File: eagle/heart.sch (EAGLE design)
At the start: 8 parts

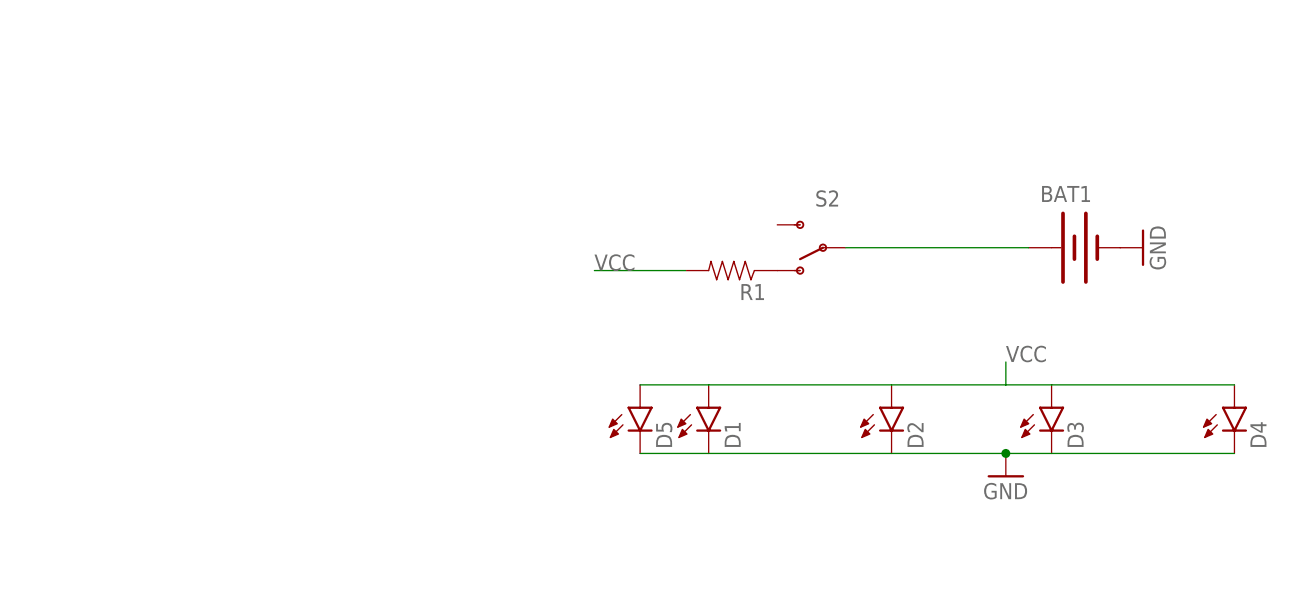
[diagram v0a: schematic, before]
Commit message: move eagle files to `eagle` dir
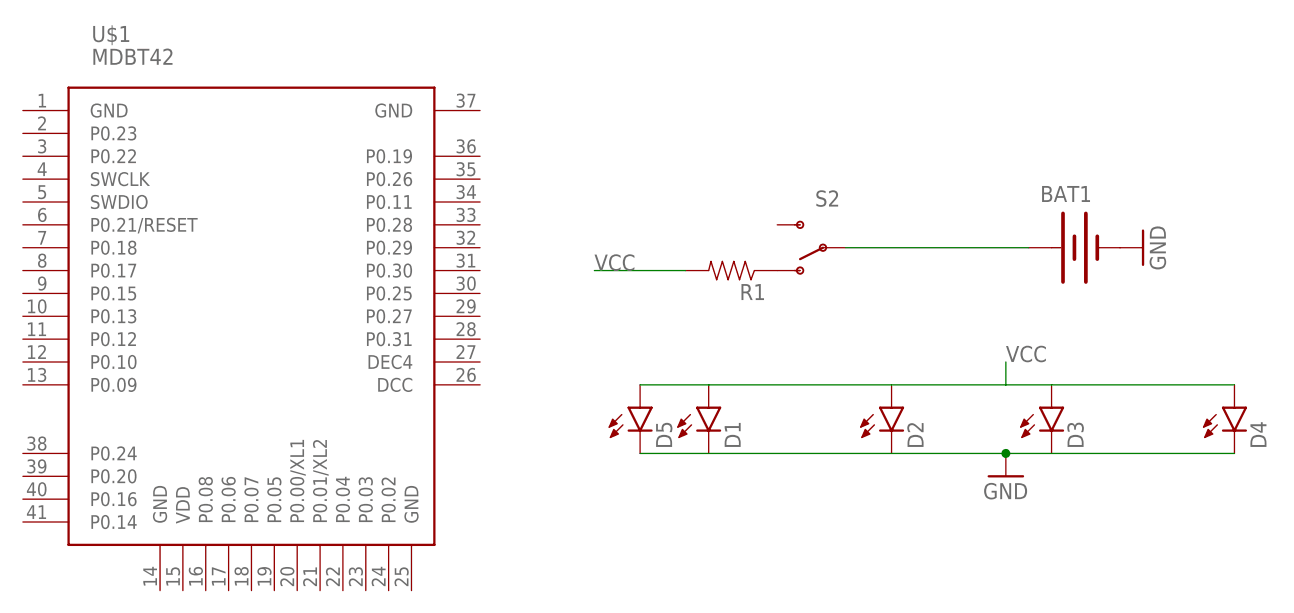
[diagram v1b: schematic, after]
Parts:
- added U$1: MDBT42, MDBT42:MDBT42
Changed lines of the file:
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@@
 <grid distance="0.1" unitdist="inch" unit="inch" style="lines" multiple="1" display="no" altdistance="0.01" altunitdist="inch" altunit="inch"/>
 <layers>
-<layer number="1" name="Top" color="4" fill="1" visible="yes" active="no"/>
-<layer number="16" name="Bottom" color="1" fill="1" visible="yes" active="no"/>
-<layer number="17" name="Pads" color="2" fill="1" visible="yes" active="no"/>
-<layer number="18" name="Vias" color="2" fill="1" visible="yes" active="no"/>
-<layer number="19" name="Unrouted" color="6" fill="1" visible="yes" active="no"/>
-<layer number="20" name="Dimension" color="15" fill="1" visible="yes" active="no"/>
-<layer number="21" name="tPlace" color="7" fill="1" visible="yes" active="no"/>
-<layer number="22" name="bPlace" color="7" fill="1" visible="yes" active="no"/>
-<layer number="23" name="tOrigins" color="15" fill="1" visible="yes" active="no"/>
-<layer number="24" name="bOrigins" color="15" fill="1" visible="yes" active="no"/>
-<layer number="25" name="tNames" color="7" fill="1" visible="yes" active="no"/>
-<layer number="26" name="bNames" color="7" fill="1" visible="yes" active="no"/>
-<layer number="27" name="tValues" color="7" fill="1" visible="yes" active="no"/>
-<layer number="28" name="bValues" color="7" fill="1" visible="yes" active="no"/>
+<layer number="1" name="Top" color="4" fill="1" visible="no" active="no"/>
+<layer number="16" name="Bottom" color="1" fill="1" visible="no" active="no"/>
+<layer number="17" name="Pads" color="2" fill="1" visible="no" active="no"/>
+<layer number="18" name="Vias" color="2" fill="1" visible="no" active="no"/>
+<layer number="19" name="Unrouted" color="6" fill="1" visible="no" active="no"/>
+<layer number="20" name="Dimension" color="15" fill="1" visible="no" active="no"/>
+<layer number="21" name="tPlace" color="7" fill="1" visible="no" active="no"/>
+<layer number="22" name="bPlace" color="7" fill="1" visible="no" active="no"/>
+<layer number="23" name="tOrigins" color="15" fill="1" visible="no" active="no"/>
+<layer number="24" name="bOrigins" color="15" fill="1" visible="no" active="no"/>
+<layer number="25" name="tNames" color="7" fill="1" visible="no" active="no"/>
+<layer number="26" name="bNames" color="7" fill="1" visible="no" active="no"/>
+<layer number="27" name="tValues" color="7" fill="1" visible="no" active="no"/>
+<layer number="28" name="bValues" color="7" fill="1" visible="no" active="no"/>
 <layer number="29" name="tStop" color="7" fill="3" visible="no" active="no"/>
 <layer number="30" name="bStop" color="7" fill="6" visible="no" active="no"/>
@@
 <layer number="35" name="tGlue" color="7" fill="4" visible="no" active="no"/>
 <layer number="36" name="bGlue" color="7" fill="5" visible="no" active="no"/>
-<layer number="37" name="tTest" color="7" fill="1" visible="yes" active="no"/>
-<layer number="38" name="bTest" color="7" fill="1" visible="yes" active="no"/>
+<layer number="37" name="tTest" color="7" fill="1" visible="no" active="no"/>
+<layer number="38" name="bTest" color="7" fill="1" visible="no" active="no"/>
 <layer number="39" name="tKeepout" color="4" fill="11" visible="no" active="no"/>
 <layer number="40" name="bKeepout" color="1" fill="11" visible="no" active="no"/>
@@
 <layer number="44" name="Drills" color="7" fill="1" visible="no" active="no"/>
 <layer number="45" name="Holes" color="7" fill="1" visible="no" active="no"/>
-<layer number="46" name="Milling" color="3" fill="1" visible="yes" active="no"/>
-<layer number="47" name="Measures" color="7" fill="1" visible="yes" active="no"/>
-<layer number="48" name="Document" color="7" fill="1" visible="yes" active="no"/>
-<layer number="49" name="Reference" color="7" fill="1" visible="yes" active="no"/>
-<layer number="50" name="dxf" color="7" fill="1" visible="yes" active="no"/>
-<layer number="51" name="tDocu" color="7" fill="1" visible="yes" active="no"/>
-<layer number="52" name="bDocu" color="7" fill="1" visible="yes" active="no"/>
-<layer number="53" name="tGND_GNDA" color="7" fill="9" visible="yes" active="no"/>
-<layer number="54" name="bGND_GNDA" color="1" fill="9" visible="yes" active="no"/>
-<layer number="56" name="wert" color="7" fill="1" visible="yes" active="no"/>
-<layer number="57" name="tCAD" color="7" fill="1" visible="yes" active="no"/>
-<layer number="59" name="tCarbon" color="7" fill="1" visible="yes" active="no"/>
-<layer number="60" name="bCarbon" color="7" fill="1" visible="yes" active="no"/>
+<layer number="46" name="Milling" color="3" fill="1" visible="no" active="no"/>
+<layer number="47" name="Measures" color="7" fill="1" visible="no" active="no"/>
+<layer number="48" name="Document" color="7" fill="1" visible="no" active="no"/>
+<layer number="49" name="Reference" color="7" fill="1" visible="no" active="no"/>
+<layer number="50" name="dxf" color="7" fill="1" visible="no" active="no"/>
+<layer number="51" name="tDocu" color="7" fill="1" visible="no" active="no"/>
+<layer number="52" name="bDocu" color="7" fill="1" visible="no" active="no"/>
+<layer number="53" name="tGND_GNDA" color="7" fill="9" visible="no" active="no"/>
+<layer number="54" name="bGND_GNDA" color="1" fill="9" visible="no" active="no"/>
+<layer number="56" name="wert" color="7" fill="1" visible="no" active="no"/>
+<layer number="57" name="tCAD" color="7" fill="1" visible="no" active="no"/>
+<layer number="59" name="tCarbon" color="7" fill="1" visible="no" active="no"/>
+<layer number="60" name="bCarbon" color="7" fill="1" visible="no" active="no"/>
 <layer number="90" name="Modules" color="5" fill="1" visible="yes" active="yes"/>
 <layer number="91" name="Nets" color="2" fill="1" visible="yes" active="yes"/>
@@
 <part name="R1" library="SparkFun-Resistors" deviceset="RESISTOR" device="0603"/>
 <part name="D5" library="SparkFun-LED" deviceset="LED" device="0603"/>
+<part name="U$1" library="MDBT42" deviceset="MDBT42" device=""/>
 </parts>
 <sheets>
@@
 <instance part="R1" gate="G$1" x="25.4" y="66.04" rot="R180"/>
 <instance part="D5" gate="G$1" x="15.24" y="50.8"/>
+<instance part="U$1" gate="G$1" x="-27.94" y="60.96"/>
 </instances>
 <busses>

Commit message: Restore original eagle files
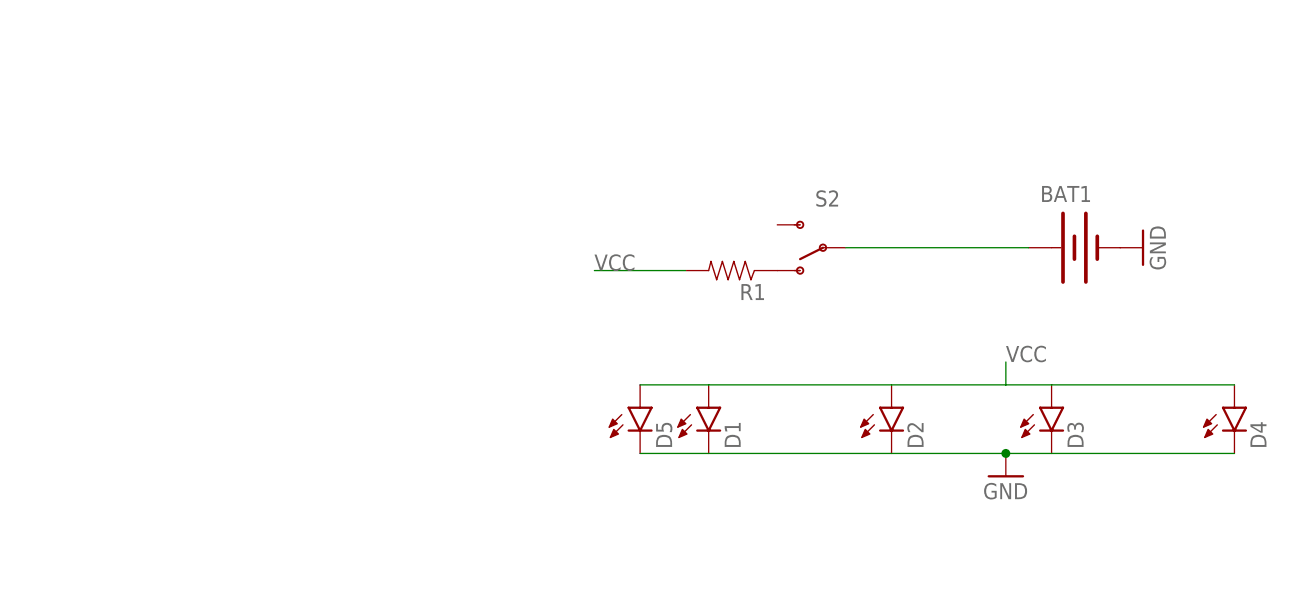
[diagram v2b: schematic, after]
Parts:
- removed U$1: MDBT42, MDBT42:MDBT42
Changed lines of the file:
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@@
 <grid distance="0.1" unitdist="inch" unit="inch" style="lines" multiple="1" display="no" altdistance="0.01" altunitdist="inch" altunit="inch"/>
 <layers>
-<layer number="1" name="Top" color="4" fill="1" visible="no" active="no"/>
-<layer number="16" name="Bottom" color="1" fill="1" visible="no" active="no"/>
-<layer number="17" name="Pads" color="2" fill="1" visible="no" active="no"/>
-<layer number="18" name="Vias" color="2" fill="1" visible="no" active="no"/>
-<layer number="19" name="Unrouted" color="6" fill="1" visible="no" active="no"/>
-<layer number="20" name="Dimension" color="15" fill="1" visible="no" active="no"/>
-<layer number="21" name="tPlace" color="7" fill="1" visible="no" active="no"/>
-<layer number="22" name="bPlace" color="7" fill="1" visible="no" active="no"/>
-<layer number="23" name="tOrigins" color="15" fill="1" visible="no" active="no"/>
-<layer number="24" name="bOrigins" color="15" fill="1" visible="no" active="no"/>
-<layer number="25" name="tNames" color="7" fill="1" visible="no" active="no"/>
-<layer number="26" name="bNames" color="7" fill="1" visible="no" active="no"/>
-<layer number="27" name="tValues" color="7" fill="1" visible="no" active="no"/>
-<layer number="28" name="bValues" color="7" fill="1" visible="no" active="no"/>
+<layer number="1" name="Top" color="4" fill="1" visible="yes" active="no"/>
+<layer number="16" name="Bottom" color="1" fill="1" visible="yes" active="no"/>
+<layer number="17" name="Pads" color="2" fill="1" visible="yes" active="no"/>
+<layer number="18" name="Vias" color="2" fill="1" visible="yes" active="no"/>
+<layer number="19" name="Unrouted" color="6" fill="1" visible="yes" active="no"/>
+<layer number="20" name="Dimension" color="15" fill="1" visible="yes" active="no"/>
+<layer number="21" name="tPlace" color="7" fill="1" visible="yes" active="no"/>
+<layer number="22" name="bPlace" color="7" fill="1" visible="yes" active="no"/>
+<layer number="23" name="tOrigins" color="15" fill="1" visible="yes" active="no"/>
+<layer number="24" name="bOrigins" color="15" fill="1" visible="yes" active="no"/>
+<layer number="25" name="tNames" color="7" fill="1" visible="yes" active="no"/>
+<layer number="26" name="bNames" color="7" fill="1" visible="yes" active="no"/>
+<layer number="27" name="tValues" color="7" fill="1" visible="yes" active="no"/>
+<layer number="28" name="bValues" color="7" fill="1" visible="yes" active="no"/>
 <layer number="29" name="tStop" color="7" fill="3" visible="no" active="no"/>
 <layer number="30" name="bStop" color="7" fill="6" visible="no" active="no"/>
@@
 <layer number="35" name="tGlue" color="7" fill="4" visible="no" active="no"/>
 <layer number="36" name="bGlue" color="7" fill="5" visible="no" active="no"/>
-<layer number="37" name="tTest" color="7" fill="1" visible="no" active="no"/>
-<layer number="38" name="bTest" color="7" fill="1" visible="no" active="no"/>
+<layer number="37" name="tTest" color="7" fill="1" visible="yes" active="no"/>
+<layer number="38" name="bTest" color="7" fill="1" visible="yes" active="no"/>
 <layer number="39" name="tKeepout" color="4" fill="11" visible="no" active="no"/>
 <layer number="40" name="bKeepout" color="1" fill="11" visible="no" active="no"/>
@@
 <layer number="44" name="Drills" color="7" fill="1" visible="no" active="no"/>
 <layer number="45" name="Holes" color="7" fill="1" visible="no" active="no"/>
-<layer number="46" name="Milling" color="3" fill="1" visible="no" active="no"/>
-<layer number="47" name="Measures" color="7" fill="1" visible="no" active="no"/>
-<layer number="48" name="Document" color="7" fill="1" visible="no" active="no"/>
-<layer number="49" name="Reference" color="7" fill="1" visible="no" active="no"/>
-<layer number="50" name="dxf" color="7" fill="1" visible="no" active="no"/>
-<layer number="51" name="tDocu" color="7" fill="1" visible="no" active="no"/>
-<layer number="52" name="bDocu" color="7" fill="1" visible="no" active="no"/>
-<layer number="53" name="tGND_GNDA" color="7" fill="9" visible="no" active="no"/>
-<layer number="54" name="bGND_GNDA" color="1" fill="9" visible="no" active="no"/>
-<layer number="56" name="wert" color="7" fill="1" visible="no" active="no"/>
-<layer number="57" name="tCAD" color="7" fill="1" visible="no" active="no"/>
-<layer number="59" name="tCarbon" color="7" fill="1" visible="no" active="no"/>
-<layer number="60" name="bCarbon" color="7" fill="1" visible="no" active="no"/>
+<layer number="46" name="Milling" color="3" fill="1" visible="yes" active="no"/>
+<layer number="47" name="Measures" color="7" fill="1" visible="yes" active="no"/>
+<layer number="48" name="Document" color="7" fill="1" visible="yes" active="no"/>
+<layer number="49" name="Reference" color="7" fill="1" visible="yes" active="no"/>
+<layer number="50" name="dxf" color="7" fill="1" visible="yes" active="no"/>
+<layer number="51" name="tDocu" color="7" fill="1" visible="yes" active="no"/>
+<layer number="52" name="bDocu" color="7" fill="1" visible="yes" active="no"/>
+<layer number="53" name="tGND_GNDA" color="7" fill="9" visible="yes" active="no"/>
+<layer number="54" name="bGND_GNDA" color="1" fill="9" visible="yes" active="no"/>
+<layer number="56" name="wert" color="7" fill="1" visible="yes" active="no"/>
+<layer number="57" name="tCAD" color="7" fill="1" visible="yes" active="no"/>
+<layer number="59" name="tCarbon" color="7" fill="1" visible="yes" active="no"/>
+<layer number="60" name="bCarbon" color="7" fill="1" visible="yes" active="no"/>
 <layer number="90" name="Modules" color="5" fill="1" visible="yes" active="yes"/>
 <layer number="91" name="Nets" color="2" fill="1" visible="yes" active="yes"/>
@@
 <part name="R1" library="SparkFun-Resistors" deviceset="RESISTOR" device="0603"/>
 <part name="D5" library="SparkFun-LED" deviceset="LED" device="0603"/>
-<part name="U$1" library="MDBT42" deviceset="MDBT42" device=""/>
 </parts>
 <sheets>
@@
 <instance part="R1" gate="G$1" x="25.4" y="66.04" rot="R180"/>
 <instance part="D5" gate="G$1" x="15.24" y="50.8"/>
-<instance part="U$1" gate="G$1" x="-27.94" y="60.96"/>
 </instances>
 <busses>
